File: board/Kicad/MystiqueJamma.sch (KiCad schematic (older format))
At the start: 143 parts, among them IC1 7805, IC10 TDA2030V, IC11 LA4425V, IC2 74HC4021D, IC3 74LS245DW, IC4 74HC4021D, IC5 CY7C1049CV33, IC6 TDA1543T, IC7 74LS245DW, IC8 TLS1233, IC9 74HC4021D, J1 Conn_01x04, K1 JAMMA-EDGE-MYSTIQUE, X2 1503_09, X4 HF15H

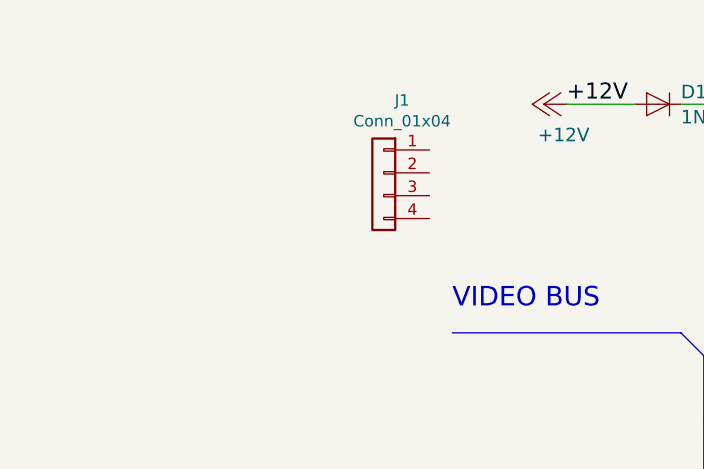
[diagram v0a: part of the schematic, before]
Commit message: Added edge cut for JTAG header
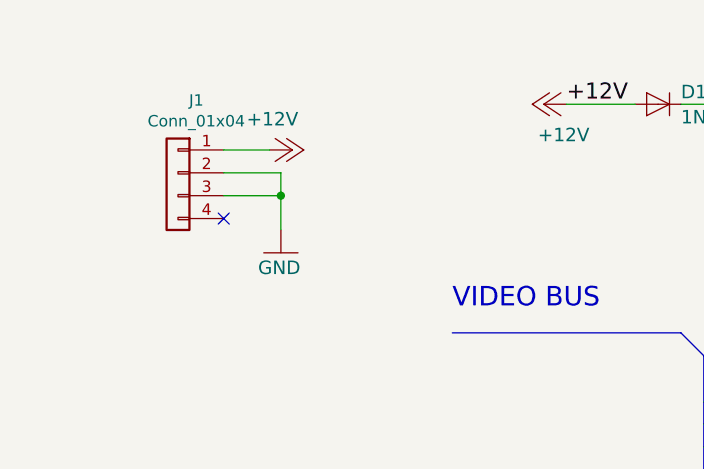
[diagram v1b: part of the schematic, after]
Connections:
- wire segments 666 -> 671
- no-connect marks 0 -> 1
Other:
- moved on the sheet: J1
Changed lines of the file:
@@
 L Connector_Generic:Conn_01x04 J1
 U 1 1 5BFE7145
-P 2300 1300
-F 0 "J1" H 2220 1617 50  0000 C CNN
-F 1 "Conn_01x04" H 2220 1526 50  0000 C CNN
-F 2 "Connector_Molex:Molex_Mega-Fit_76829-0004_2x02_P5.70mm_Vertical" H 2300 1300 50  0001 C CNN
-F 3 "~" H 2300 1300 50  0001 C CNN
-	1    2300 1300
+P 1400 1300
+F 0 "J1" H 1320 1617 50  0000 C CNN
+F 1 "Conn_01x04" H 1320 1526 50  0000 C CNN
+F 2 "Connector_Molex:Molex_Mega-Fit_76829-0004_2x02_P5.70mm_Vertical" H 1400 1300 50  0001 C CNN
+F 3 "~" H 1400 1300 50  0001 C CNN
+	1    1400 1300
 	-1   0    0    -1
 $EndComp
+$Comp
+L MystiqueJamma-eagle-import:GND #GND0101
+U 1 0 5BD7AF12
+P 1850 1650
+F 0 "#GND0101" H 1850 1650 50  0001 C CNN
+F 1 "GND" H 1750 1550 59  0000 L BNN
+F 2 "" H 1850 1650 50  0001 C CNN
+F 3 "" H 1850 1650 50  0001 C CNN
+	1    1850 1650
+	1    0    0    -1
+$EndComp
+$Comp
+L MystiqueJamma-eagle-import:+12V #P+0103
+U 1 0 5BF2CAB6
+P 1900 1200
+F 0 "#P+0103" H 1900 1200 50  0001 C CNN
+F 1 "+12V" V 1800 1000 59  0000 L BNN
+F 2 "" H 1900 1200 50  0001 C CNN
+F 3 "" H 1900 1200 50  0001 C CNN
+	1    1900 1200
+	0    1    1    0
+$EndComp
+Wire Wire Line
+	1600 1200 1800 1200
+Wire Wire Line
+	1600 1300 1850 1300
+Wire Wire Line
+	1850 1300 1850 1400
+Wire Wire Line
+	1600 1400 1850 1400
+Connection ~ 1850 1400
+Wire Wire Line
+	1850 1400 1850 1550
+NoConn ~ 1600 1500
 Wire Bus Line
 	1900 10700 1900 11200

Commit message: Edge connector pins associated with shift registers
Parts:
- added D4, D5: 4148, MystiqueJamma:SOD80C, symbol MystiqueJamma-eagle-import:DIODE-SOD80C
- added J2: Conn_02x10_Odd_Even, Connector_PinHeader_2.54mm:PinHeader_2x10_P2.54mm_Vertical, symbol Connector_Generic:Conn_02x10_Odd_Even
- added R94, R95: 330, MystiqueJamma:M1206, symbol MystiqueJamma-eagle-import:R-US_M1206
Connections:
- net labels added: COINSW2, COIN_CT1, COIN_CT2, P2B1, P2B2, P2B3, P2B4, P2B5, P2DW, P2LH, P2RH, P2START, P2UP, SERVICE_SW, TILT
- net labels removed: N$46, N$47, N$61, N$62, N$63, N$64, N$65, N$66, N$67, N$68, N$69, N$70, N$72, N$73, N$74, N$75, N$76, N$77, N$78, N$79, N$80, N$81, N$82
- wire segments 671 -> 694
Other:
- moved on the sheet: J1

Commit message: First completed layout
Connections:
- net +5V: no longer K1.3 (+5V@1), K1.4 (+5V@2), K1.C (+5V@1), K1.D (+5V@2)
- net IO_100: now reaches J2.1 (Pin_1)
- net IO_100: now also U$3.I0_100 (39)
- net IO_71: now reaches J2.10 (Pin_10)
- net IO_71: now also U$3.I0_71 (32)
- net IO_68: now reaches J2.11 (Pin_11)
- net IO_68: now also U$3.I0_68 (29)
- net IO_69: now reaches J2.12 (Pin_12)
- net IO_69: now also U$3.I0_69 (30)
- net IO_66: now reaches J2.13 (Pin_13)
- net IO_66: now also U$3.I0_66 (27)
- net IO_67: now reaches J2.14 (Pin_14)
- net IO_67: now also U$3.I0_67 (28)
- net IO_113: now reaches J2.15 (Pin_15)
- net IO_113: now also U$3.I0_113 (29)
- net IO_65: now reaches J2.16 (Pin_16)
- net IO_65: now also U$3.I0_65 (26)
- net IO_111: now reaches J2.17 (Pin_17)
- net IO_111: now also U$3.I0_111 (31)
- net IO_114: now reaches J2.18 (Pin_18)
- net IO_114: now also U$3.I0_114 (30)
- net AUD-IN: now reaches J2.20 (Pin_20)
- net AUD-IN: now also C25.+, IC10.1 (+IN), IC11.1 (+IN), R3.2
- net IO_91: now reaches J2.3 (Pin_3)
- net IO_91: now also U$3.I0_91 (37)
- net IO_99: now reaches J2.4 (Pin_4)
- net IO_99: now also U$3.I0_99 (38)
- net IO_89: now reaches J2.5 (Pin_5)
- net IO_89: now also U$3.I0_89 (35)
- net IO_90: now reaches J2.6 (Pin_6)
- net IO_90: now also U$3.I0_90 (36)
- net IO_72: now reaches J2.7 (Pin_7)
- net IO_72: now also U$3.I0_72 (33)
- net IO_88: now reaches J2.8 (Pin_8)
- net IO_88: now also U$3.I0_88 (34)
- net IO_70: now reaches J2.9 (Pin_9)
- net IO_70: now also U$3.I0_70 (31)
- net -5V renamed NC5
- net NC5: no longer K1.E (-5V)
- new net NC3: K1.3 (+5V@1)
- new net NC4: K1.4 (+5V@2)
- new net NCC: K1.C (+5V@1)
- new net NCD: K1.D (+5V@2)
- new net NCE: K1.E (-5V)
- no-connect marks 1 -> 10
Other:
- moved on the sheet: J2

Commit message: routing and footprints enhancement
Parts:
- added J3: FPGA PWR, Connector_PinHeader_2.54mm:PinHeader_1x02_P2.54mm_Horizontal, symbol Connector:Conn_01x02_Male
- renumbered U$3 to EVB1, U$2 to J4, X2 to J5, X4 to J6
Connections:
- net labels removed: COIN_CT1, COIN_CT2
- wire segments 713 -> 714
- no-connect marks 10 -> 29
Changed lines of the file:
@@
 Text Label 16900 8700 2    70   ~ 0
 GND
-Wire Wire Line
-	17300 10200 16700 10200
 Text Label 16700 10200 2    70   ~ 0
 GND
@@
 	5700 7700 5800 7700
 Wire Wire Line
-	5500 7800 5700 7800
-Wire Wire Line
 	5700 7800 5700 7700
 Connection ~ 5700 7700
@@
 $EndComp
 $Comp
-L MystiqueJamma-eagle-import:SDMMC06132 U$2
+L MystiqueJamma-eagle-import:SDMMC06132 J4
 U 1 0 87B7DF34
 P 9300 8600
-F 0 "U$2" H 9300 8600 50  0001 C CNN
+F 0 "J4" H 9000 9600 59  0000 C CNN
 F 1 "SDMMC06132" H 9300 8600 50  0001 C CNN
 F 2 "MystiqueJamma:06132" H 9300 8600 50  0001 C CNN
@@
 $EndComp
 $Comp
-L MystiqueJamma-eagle-import:1503_09 X2
+L MystiqueJamma-eagle-import:1503_09 J5
 U 1 0 EE6A8C5B
 P 8900 11000
-F 0 "X2" H 8800 11250 59  0000 L BNN
+F 0 "J5" H 8800 11250 59  0000 L BNN
 F 1 "1503_09" H 8800 10700 59  0000 L BNN
 F 2 "MystiqueJamma:1503_09" H 8900 11000 50  0001 C CNN
@@
 $EndComp
 $Comp
-L MystiqueJamma-eagle-import:C4E6-K U$3
+L MystiqueJamma-eagle-import:C4E6-K EVB1
 U 1 0 6E1B97F5
 P 1800 8700
-F 0 "U$3" H 1650 9730 59  0000 L BNN
+F 0 "EVB1" H 1650 9730 59  0000 L BNN
 F 1 "C4E6-K" H 1650 7500 59  0000 L BNN
 F 2 "MystiqueJamma:E6V33_BELOW" H 1800 8700 50  0001 C CNN
@@
 $EndComp
 $Comp
-L MystiqueJamma-eagle-import:C4E6-K U$3
+L MystiqueJamma-eagle-import:C4E6-K EVB1
 U 2 0 6E1B97F9
 P 1800 4100
-F 0 "U$3" H 1650 5130 59  0000 L BNN
+F 0 "EVB1" H 1650 5130 59  0000 L BNN
 F 1 "C4E6-K" H 1650 2900 59  0000 L BNN
 F 2 "MystiqueJamma:E6V33_BELOW" H 1800 4100 50  0001 C CNN
@@
 $EndComp
 $Comp
-L MystiqueJamma-eagle-import:HF15H X4
+L MystiqueJamma-eagle-import:HF15H J6
 U 1 0 38D8100C
 P 7500 5200
-F 0 "X4" H 7350 5750 59  0000 L BNN
+F 0 "J6" H 7350 5750 59  0000 L BNN
 F 1 "HF15H" H 7325 4475 59  0000 L BNN
 F 2 "MystiqueJamma:HDF15H" H 7500 5200 50  0001 C CNN
@@
 U 1 0 F6216840
 P 12400 4700
-F 0 "R57" V 12165 4550 59  0000 L BNN
-F 1 "TRIM_EU-B90P" V 12250 4550 59  0000 L BNN
+F 0 "R57" H 12100 4750 59  0000 L BNN
+F 1 "TRIM_EU-B90P" H 11600 4600 59  0000 L BNN
 F 2 "MystiqueJamma:SP19L" H 12400 4700 50  0001 C CNN
 F 3 "" H 12400 4700 50  0001 C CNN
@@
 U 1 0 86216CFC
 P 14400 4700
-F 0 "R58" V 14165 4550 59  0000 L BNN
-F 1 "TRIM_EU-B90P" V 14250 4550 59  0000 L BNN
+F 0 "R58" H 14100 4750 59  0000 L BNN
+F 1 "TRIM_EU-B90P" H 13600 4650 59  0000 L BNN
 F 2 "MystiqueJamma:SP19L" H 14400 4700 50  0001 C CNN
 F 3 "" H 14400 4700 50  0001 C CNN
@@
 TILT
 Wire Wire Line
-	17300 6700 16700 6700
-Wire Wire Line
-	17300 10000 16700 10000
-Wire Wire Line
 	15000 11300 15400 11300
 Text Label 15400 11300 0    50   ~ 0
@@
 Wire Wire Line
 	13600 12450 13600 12550
-Text Label 16700 6700 2    70   ~ 0
-COIN_CT1
-Text Label 16700 10000 2    70   ~ 0
-COIN_CT2
 Text Label 16700 10300 2    70   ~ 0
 GND
@@
 Text Label 3100 4600 2    50   ~ 0
 IO_114
+$Comp
+L Connector:Conn_01x02_Male J3
+U 1 1 5BED1A57
+P 1800 2350
+F 0 "J3" H 1906 2528 50  0000 C CNN
+F 1 "FPGA PWR" H 1906 2437 50  0000 C CNN
+F 2 "Connector_PinHeader_2.54mm:PinHeader_1x02_P2.54mm_Horizontal" H 1800 2350 50  0001 C CNN
+F 3 "~" H 1800 2350 50  0001 C CNN
+	1    1800 2350
+	1    0    0    -1
+$EndComp
+$Comp
+L MystiqueJamma-eagle-import:GND #GND0104
+U 1 0 5BED32BE
+P 2100 2600
+F 0 "#GND0104" H 2100 2600 50  0001 C CNN
+F 1 "GND" H 2000 2500 59  0000 L BNN
+F 2 "" H 2100 2600 50  0001 C CNN
+F 3 "" H 2100 2600 50  0001 C CNN
+	1    2100 2600
+	1    0    0    -1
+$EndComp
+$Comp
+L MystiqueJamma-eagle-import:+5V #P+0104
+U 1 0 5C0210A4
+P 2450 2350
+F 0 "#P+0104" H 2450 2350 50  0001 C CNN
+F 1 "+5V" V 2350 2150 59  0000 L BNN
+F 2 "" H 2450 2350 50  0001 C CNN
+F 3 "" H 2450 2350 50  0001 C CNN
+	1    2450 2350
+	0    1    1    0
+$EndComp
+Wire Wire Line
+	2350 2350 2000 2350
+Wire Wire Line
+	2000 2450 2100 2450
+Wire Wire Line
+	2100 2450 2100 2500
+NoConn ~ 11800 10600
+NoConn ~ 11800 10800
+NoConn ~ 11800 7100
+NoConn ~ 11800 7300
+NoConn ~ 11800 8800
+NoConn ~ 11800 9000
+NoConn ~ 8800 8600
+NoConn ~ 8800 8700
+NoConn ~ 8800 7800
+NoConn ~ 8800 7900
+NoConn ~ 8800 8000
+Wire Wire Line
+	5500 7800 5700 7800
+NoConn ~ 17300 9500
+NoConn ~ 17300 9600
+NoConn ~ 17300 9700
+Wire Wire Line
+	16700 10200 17300 10200
+NoConn ~ 17300 6700
+NoConn ~ 17300 10000
+NoConn ~ 17300 6300
+NoConn ~ 17300 6200
+NoConn ~ 17300 6400
 Wire Bus Line
-	1900 10700 1900 11200
-Wire Bus Line
-	11100 6900 11100 12200
+	3700 2100 3700 4800
 Wire Bus Line
-	7600 8000 7600 8500
+	3900 7200 3900 9500
 Wire Bus Line
 	6000 7300 6000 9100
 Wire Bus Line
-	3900 7200 3900 9500
+	7600 8000 7600 8500
 Wire Bus Line
-	3700 2100 3700 4800
+	11100 6900 11100 12200
+Wire Bus Line
+	1900 10700 1900 11200
 $EndSCHEMATC

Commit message: Added Mini DIN6 Connector
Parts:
- added C31: 100nF, MystiqueJamma:C1206, symbol MystiqueJamma-eagle-import:C-USC1206
- added D6, D7, D8, D9: 4148, MystiqueJamma:SOD80C, symbol MystiqueJamma-eagle-import:DIODE-SOD80C
- added J7: Mini-DIN-6, r_mini_din:Mini_din6, symbol MystiqueJamma-rescue:Mini-DIN-6-Connector
- added R96, R97: 2K2, MystiqueJamma:M1206, symbol MystiqueJamma-eagle-import:R-US_M1206
- added R98, R99: 120, MystiqueJamma:M1206, symbol MystiqueJamma-eagle-import:R-US_M1206
- J3: symbol Connector:Conn_01x02_Male -> MystiqueJamma-rescue:Conn_01x02_Male-Connector
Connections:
- net labels added: PS2CK, PS2DAT
- net labels removed: IO_111, IO_114
- wire segments 714 -> 747

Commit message: Removed old directory updated schematics
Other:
- note removed: "Mystique JAMMA"
- moved on the sheet: C1, C10, C11, C12, C13, C14, C15, C16, C17, C18, C19, C2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

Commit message: Updated component values
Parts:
- C22: value CPOL-USE2-4 -> 22u
- C25: value CPOL-USE2-4 -> 10uF
- C26: value CPOL-USE2-4 -> 2u2
- C28: value 100nF -> 220nF
- D2, D3: value DIODE-SOD80C -> 1N4004
- R1, R2, R3: value 470 -> 100k
- R28, R29, R4: value 470 -> 4k7
- R41: value 330 -> 420
- R42: value 330 -> 785
- R43: value 330 -> 1380
- R44: value 330 -> 2230
- R5: value 470 -> 150k
- R53, R54, R55, R70, R71, R72, R73, R74, R75, R76, R77, R78, R79, R80, R81, R82, R83, R84, R85, R86, R87, R88, R89, R90, R91, R92, R93, R94: value 330 -> 10k
- R56: value 330 -> 5k
- R57, R58: value TRIM_EU-B90P -> 5k
- R59, R60, R61: value 330 -> 430
- R6: value 470 -> 1R
- R9: value VOLUME-POT -> 50k
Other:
- moved on the sheet: R98

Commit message: Added second SRAM, Match FPGA IO usage with board available pins
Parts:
- removed J2: Conn_02x10_Odd_Even, Connector_PinHeader_2.54mm:PinHeader_2x10_P2.54mm_Vertical, symbol Connector_Generic:Conn_02x10_Odd_Even
- added C32: 100nF, MystiqueJamma:C1206, symbol MystiqueJamma-eagle-import:C-USC1206
- added C33: 10n, MystiqueJamma:C1206, symbol MystiqueJamma-eagle-import:C-USC1206
- added D10: 4148, MystiqueJamma:SOD80C, symbol MystiqueJamma-eagle-import:DIODE-SOD80C
- added IC12: CY7C1049CV33, MystiqueJamma:SOJV36-400, symbol MystiqueJamma-eagle-import:CY7C1049CV33
- added R100: 4k7, MystiqueJamma:M1206, symbol MystiqueJamma-eagle-import:R-US_M1206
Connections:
- net IO_100 is gone; now on net SD_CS: EVB1.I0_100 (39)
- net IO_113 is gone; now on net SRAM_A18: EVB1.I0_113 (29)
- net IO_65 is gone; now on net SRAM_A12: EVB1.I0_65 (26)
- net IO_66 is gone; now on net SRAM_IO4: EVB1.I0_66 (27)
- net IO_67 is gone; now on net SRAM_A14: EVB1.I0_67 (28)
- net IO_68 is gone; now on net CNTR_CK_LAT: EVB1.I0_68 (29)
- net IO_69 is gone; now on net SRAM_IO5: EVB1.I0_69 (30)
- net IO_71 is gone; now on net I2S_DATA: EVB1.I0_71 (32)
- net IO_88 is gone; now on net SD_DATAOUT: EVB1.I0_88 (34)
- net IO_99 is gone; now on net SD_DATAIN: EVB1.I0_99 (38)
- net +3V3: now also C32.1, IC12.27 (+3V@2), IC12.9 (+3V@1)
- net B0: now also EVB1.I0_30 (2); no longer EVB1.I0_3 (4)
- net B1: now also EVB1.I0_28 (1); no longer EVB1.I0_7 (3)
- net B2: now also EVB1.I0_32 (4); no longer EVB1.I0_10 (2)
- net B3: now also EVB1.I0_31 (3); no longer EVB1.I0_11 (1)
- net CNTR_DAT: now also EVB1.I0_53 (19); no longer EVB1.I0_33 (5)
- net G1: now also EVB1.I0_7 (3); no longer EVB1.I0_144 (7)
- net G2: now also EVB1.I0_10 (2); no longer EVB1.I0_1 (6)
- net G3: now also EVB1.I0_11 (1); no longer EVB1.I0_2 (5)
- net GND: now also IC5.31 (OE), C32.2, IC12.10 (GND@1), IC12.28 (GND@2), IC12.31 (OE)
- net HSY: now also EVB1.I0_33 (5), IC7.7 (A6); no longer EVB1.I0_30 (2)
- net I2S_BCK: now also EVB1.I0_103 (38); no longer EVB1.I0_110 (34)
- net I2S_DATA: no longer EVB1.I0_112 (32)
- net JAMMA-CSYNC: now also R46.2; no longer R48.2
- net PS2CK: now also EVB1.I0_135 (14); no longer EVB1.I0_111 (31)
- net PS2DAT: now also EVB1.I0_136 (13); no longer EVB1.I0_114 (30)
- net R1: now also EVB1.I0_142 (9); no longer EVB1.I0_138 (11)
- net R3: now also EVB1.I0_144 (7); no longer EVB1.I0_142 (9)
- net SD_CS: no longer EVB1.I0_104 (35)
- net SD_DATAIN: no longer EVB1.I0_105 (36)
- net SD_DATAOUT: no longer EVB1.I0_103 (38)
- net SRAM_A0: now also EVB1.I0_114 (30), IC12.1 (A0); no longer EVB1.I0_115 (27)
- net SRAM_A1: now also EVB1.I0_115 (27), IC12.2 (A1); no longer EVB1.I0_119 (28)
- net SRAM_A10: now also EVB1.I0_60 (24), IC12.20 (A10); no longer EVB1.I0_50 (14)
- net SRAM_A11: now also EVB1.I0_59 (23), IC12.21 (A11); no longer EVB1.I0_44 (11)
- net SRAM_A12: now also IC12.22 (A12); no longer EVB1.I0_46 (12)
- net SRAM_A13: now also EVB1.I0_64 (25), IC12.23 (A13); no longer EVB1.I0_42 (9)
- net SRAM_A14: now also IC12.24 (A14); no longer EVB1.I0_43 (10)
- net SRAM_A15: now also EVB1.I0_110 (34), IC12.32 (A15); no longer EVB1.I0_136 (13)
- net SRAM_A16: now also EVB1.I0_111 (31), IC12.33 (A16); no longer EVB1.I0_135 (14)
- net SRAM_A17: now also EVB1.I0_112 (32), IC12.34 (A17); no longer EVB1.I0_133 (15)
- net SRAM_A18: now also IC12.35 (A18); no longer EVB1.I0_132 (16)
- net SRAM_A2: now also EVB1.I0_119 (28), IC12.3 (A2); no longer EVB1.I0_120 (25)
- net SRAM_A3: now also EVB1.I0_120 (25), IC12.4 (A3); no longer EVB1.I0_121 (26)
- net SRAM_A4: now also EVB1.I0_121 (26), IC12.5 (A4); no longer EVB1.I0_124 (23)
- net SRAM_A5: now also EVB1.I0_44 (11), IC12.14 (A5); no longer EVB1.I0_55 (21)
- net SRAM_A6: now also EVB1.I0_50 (14), IC12.15 (A6); no longer EVB1.I0_58 (22)
- net SRAM_A7: now also EVB1.I0_49 (13), IC12.16 (A7); no longer EVB1.I0_59 (23)
- net SRAM_A8: now also EVB1.I0_51 (15), IC12.17 (A8); no longer EVB1.I0_60 (24)
- net SRAM_A9: now also EVB1.I0_58 (22), IC12.18 (A9); no longer EVB1.I0_64 (25)
- net SRAM_IO0: now also EVB1.I0_133 (15), IC12.7 (I/O00); no longer EVB1.I0_126 (21)
- net SRAM_IO1: now also EVB1.I0_132 (16), IC12.8 (I/O01); no longer EVB1.I0_127 (22)
- net SRAM_IO2: now also EVB1.I0_43 (10), IC12.11 (I/O02); no longer EVB1.I0_51 (15)
- net SRAM_IO3: now also EVB1.I0_42 (9), IC12.12 (I/O03); no longer EVB1.I0_53 (19)
- net SRAM_IO4: now also IC12.25 (I/O04); no longer EVB1.I0_49 (13)
- net SRAM_IO5: now also IC12.26 (I/O05); no longer EVB1.I0_52 (16)
- net SRAM_IO6: now also EVB1.I0_105 (36), IC12.29 (I/O06); no longer EVB1.I0_128 (19)
- net SRAM_IO7: now also EVB1.I0_106 (33), IC12.30 (I/O07); no longer EVB1.I0_129 (20)
- net SRAM_WE: now also EVB1.I0_46 (12), IC12.13 (WE); no longer EVB1.I0_54 (20)
- net VGA-VSYNC: now also R48.2; no longer R46.2
- net VSY: now also EVB1.I0_39 (8), IC7.8 (A7), IC7.9 (A8); no longer EVB1.I0_28 (1), IC7.7 (A6)
- net CNTR_CLK renamed CNTR_CK_LAT
- net CNTR_CK_LAT: now also D10.C, R100.1; no longer EVB1.I0_34 (6)
- net CNTR_LATCH renamed LATCH
- net LATCH: now also C33.1, D10.A, R100.2; no longer EVB1.I0_38 (7)
- removed net CSY: EVB1.I0_32 (4), IC7.8 (A7)
- removed net GATE: EVB1.I0_31 (3), IC7.9 (A8)
- net IO_70: no longer names the net of EVB1.I0_70 (31)
- net IO_72 renamed SD_CNT_SCLK
- net SD_CNT_SCLK: now also J4.5 (SCLK)
- net IO_89: no longer names the net of EVB1.I0_89 (35)
- net IO_90: no longer names the net of EVB1.I0_90 (36)
- net IO_91: no longer names the net of EVB1.I0_91 (37)
- net IS2_WS renamed I2S_WS
- net I2S_WS: now also EVB1.I0_101 (37); no longer EVB1.I0_106 (33)
- removed net SD_SCLK: EVB1.I0_101 (37), J4.5 (SCLK)
- net SRAM_CE renamed SRAM_CE1
- removed net SRAM_OE: EVB1.I0_39 (8), IC5.31 (OE)
- new net SRAM_CE2: EVB1.I0_104 (35), IC12.6 (CE)
- no-connect marks 29 -> 47
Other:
- note added: "(IC12)"
- moved on the sheet: C1, C17, C18, C19, C2, C20, C21, C29, C30, C5, C7, D1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
